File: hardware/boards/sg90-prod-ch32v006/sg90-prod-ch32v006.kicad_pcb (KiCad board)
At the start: 4 copper layers, 12.1 x 9.6 mm, 31 parts, among them J1 Servo Input, J2 Motor, J3 Debug, J4 Potentiometer, U1 TLV76733DRVR, U4 DRV8837, U5 CH32V006F8U6, U6 74LVC2G241GS,115

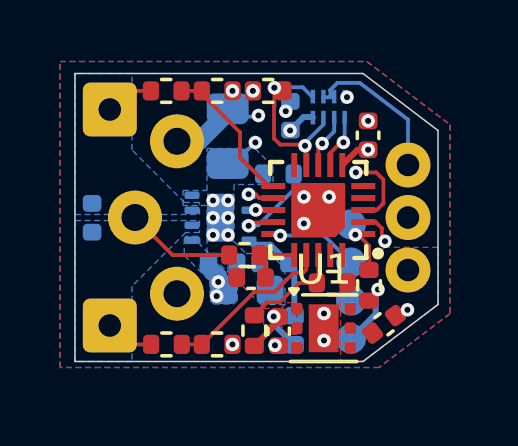
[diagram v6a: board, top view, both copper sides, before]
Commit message: fix ch32v006 footprint. it should be smd instead of th
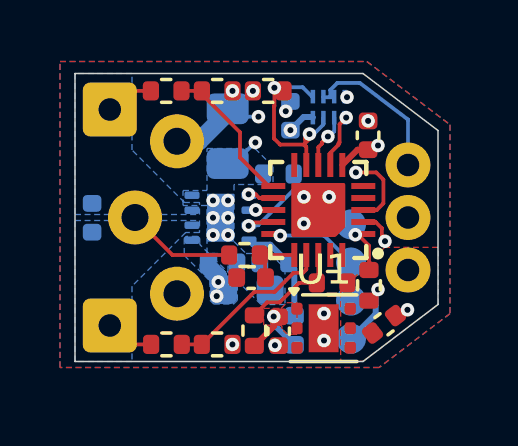
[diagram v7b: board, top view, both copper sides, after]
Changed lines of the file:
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@@
 		(sheetname "/")
 		(sheetfile "sg90-prod-ch32v006.kicad_sch")
-		(attr through_hole)
+		(attr smd)
 		(fp_line
 			(start 1.6 -1.6)
@@
 			(layer "F.Fab")
 		)
+		(fp_text user "${REFERENCE}"
+			(at 0 0 90)
+			(layer "F.Fab")
+			(effects
+				(font
+					(size 1 1)
+					(thickness 0.15)
+				)
+			)
+		)
 		(pad "1" smd rect
 			(at -0.8 1.5 90)
@@
 	)
 	(via
-		(at 109.770389 92.739435)
+		(at 110.1 92.6)
 		(size 0.45)
 		(drill 0.2)
@@
 	)
 	(via
-		(at 107.17 92.1)
+		(at 107.18 92.09)
 		(size 0.45)
 		(drill 0.2)
@@
 	)
 	(segment
-		(start 107.91 91.65)
-		(end 107.93 91.67)
-		(width 0.2)
-		(layer "B.Cu")
-		(net 6)
-	)
-	(segment
 		(start 110.1 97.4)
 		(end 110.025003 97.474997)
@@
 	)
 	(segment
-		(start 107.17 92.1)
-		(end 107.62 91.65)
+		(start 107.91 91.65)
+		(end 107.93 91.67)
 		(width 0.2)
 		(layer "B.Cu")
@@
 	)
 	(segment
-		(start 110.025003 98.214997)
-		(end 109.2 99.04)
+		(start 107.18 92.09)
+		(end 107.62 91.65)
 		(width 0.2)
 		(layer "B.Cu")
@@
 	)
 	(segment
+		(start 110.025003 98.214997)
+		(end 109.2 99.04)
+		(width 0.2)
+		(layer "B.Cu")
+		(net 6)
+	)
+	(segment
 		(start 106.622843 98.3)
 		(end 106.622843 98.557843)
@@
 	)
 	(segment
-		(start 108.238595 92.532886)
-		(end 108.237181 92.532886)
+		(start 108.237181 92.532886)
+		(end 108.11 92.660067)
 		(width 0.127)
 		(layer "F.Cu")
@@
 	)
 	(segment
-		(start 108.237181 92.532886)
-		(end 108.11 92.660067)
+		(start 108.430004 92.299417)
+		(end 108.237181 92.49224)
 		(width 0.127)
 		(layer "F.Cu")
@@
 		(net 7)
 	)
+	(segment
+		(start 108.237181 92.49224)
+		(end 108.237181 92.532886)
+		(width 0.127)
+		(layer "F.Cu")
+		(net 7)
+	)
 	(via
-		(at 108.238595 92.532886)
+		(at 108.430004 92.299417)
 		(size 0.45)
 		(drill 0.2)
@@
 	)
 	(segment
-		(start 108.238595 92.532886)
+		(start 108.472064 92.299417)
 		(end 108.64 92.131481)
 		(width 0.127)
@@
 	)
 	(segment
-		(start 108.782793 92.576294)
-		(end 108.51 92.849087)
+		(start 108.430004 92.299417)
+		(end 108.472064 92.299417)
+		(width 0.127)
+		(layer "B.Cu")
+		(net 7)
+	)
+	(segment
+		(start 108.818504 92.497998)
+		(end 108.782793 92.533709)
+		(width 0.127)
+		(layer "F.Cu")
+		(net 8)
+	)
+	(segment
+		(start 108.51 92.849087)
+		(end 108.51 93.25)
 		(width 0.127)
 		(layer "F.Cu")
@@
 	)
 	(segment
-		(start 108.51 92.849087)
-		(end 108.51 93.25)
+		(start 109.040002 91.67)
+		(end 108.818504 91.891498)
 		(width 0.127)
 		(layer "F.Cu")
@@
 	)
 	(segment
-		(start 108.946502 92.497998)
+		(start 108.818504 91.891498)
 		(end 108.818504 92.497998)
 		(width 0.127)
@@
 	)
 	(segment
-		(start 108.818504 92.497998)
-		(end 108.782793 92.533709)
+		(start 108.782793 92.576294)
+		(end 108.51 92.849087)
 		(width 0.127)
 		(layer "F.Cu")
@@
 	)
 	(via
-		(at 108.946502 92.497998)
+		(at 109.040002 91.67)
 		(size 0.45)
 		(drill 0.2)
@@
 	)
 	(segment
-		(start 108.99 92.4545)
-		(end 108.99 91.7)
+		(start 109.040002 91.67)
+		(end 109.02 91.67)
 		(width 0.127)
 		(layer "B.Cu")
@@
 	)
 	(segment
-		(start 108.946502 92.497998)
-		(end 108.99 92.4545)
+		(start 109.02 91.67)
+		(end 108.99 91.7)
 		(width 0.127)
 		(layer "B.Cu")
@@
 	)
 	(via
-		(at 106.115 91.6)
+		(at 106.115 91.64)
 		(size 0.45)
 		(drill 0.2)
@@
 	)
 	(segment
-		(start 106.115 91.645)
-		(end 107.551498 93.081498)
+		(start 106.115 91.64)
+		(end 106.115 92.015)
 		(width 0.127)
 		(layer "In2.Cu")
@@
 	)
 	(segment
-		(start 110.332581 95.52588)
-		(end 110.332581 95.790872)
-		(width 0.127)
-		(layer "In2.Cu")
-		(net 19)
-	)
-	(segment
-		(start 110.1855 93.732476)
-		(end 110.1855 95.378799)
+		(start 106.115 92.015)
+		(end 107.181498 93.081498)
 		(width 0.127)
 		(layer "In2.Cu")
@@
 	)
 	(segment
-		(start 107.551498 93.081498)
+		(start 107.181498 93.081498)
 		(end 109.534522 93.081498)
 		(width 0.127)
@@
 	)
 	(segment
-		(start 106.115 91.6)
-		(end 106.115 91.645)
+		(start 110.332581 95.52588)
+		(end 110.332581 95.790872)
 		(width 0.127)
 		(layer "In2.Cu")
@@
 	)
 	(segment
-		(start 107.627679 92.570124)
-		(end 107.666649 92.609094)
+		(start 110.1855 93.732476)
+		(end 110.1855 95.378799)
+		(width 0.127)
+		(layer "In2.Cu")
+		(net 19)
+	)
+	(segment
+		(start 107.71 92.64793)
+		(end 107.71 93.25)
 		(width 0.127)
 		(layer "F.Cu")
@@
 	)
 	(segment
-		(start 106.646135 90.675)
+		(start 107.815 92.21753)
+		(end 107.815 92.382803)
+		(width 0.127)
+		(layer "F.Cu")
+		(net 20)
+	)
+	(segment
+		(start 106.635025 91.296663)
 		(end 106.646135 91.285553)
 		(width 0.127)
@@
 	(segment
 		(start 106.646135 91.285553)
-		(end 106.635025 91.296663)
+		(end 106.646135 90.675)
+		(width 0.127)
+		(layer "F.Cu")
+		(net 20)
+	)
+	(segment
+		(start 106.839144 92.570124)
+		(end 106.635025 92.366005)
 		(width 0.127)
 		(layer "F.Cu")
@@
 	(segment
 		(start 106.635025 92.366005)
-		(end 106.839144 92.570124)
+		(end 106.635025 91.296663)
 		(width 0.127)
 		(layer "F.Cu")
@@
 	)
 	(segment
-		(start 106.839144 92.570124)
-		(end 107.627679 92.570124)
+		(start 107.815 92.21753)
+		(end 107.671164 92.361366)
 		(width 0.127)
 		(layer "F.Cu")
@@
 	)
 	(segment
-		(start 107.666649 92.609094)
+		(start 107.671164 92.361366)
 		(end 107.671164 92.609094)
 		(width 0.127)
@@
 	)
 	(segment
-		(start 106.635025 91.296663)
-		(end 106.635025 92.366005)
+		(start 107.815 92.382803)
+		(end 107.627679 92.570124)
 		(width 0.127)
 		(layer "F.Cu")
@@
 	)
 	(segment
-		(start 107.71 92.64793)
-		(end 107.71 93.25)
+		(start 107.627679 92.570124)
+		(end 106.839144 92.570124)
 		(width 0.127)
 		(layer "F.Cu")
@@
 	)
 	(via
-		(at 107.666649 92.609094)
+		(at 107.815 92.21753)
 		(size 0.45)
 		(drill 0.2)
@@
 	)
 	(segment
-		(start 108.28 91.9)
-		(end 108.28 91.67)
+		(start 106.646135 90.675)
+		(end 106.662635 90.6585)
 		(width 0.127)
 		(layer "B.Cu")
@@
 	)
 	(segment
-		(start 106.646135 90.675)
-		(end 106.662635 90.6585)
+		(start 107.96247 92.21753)
+		(end 108.28 91.9)
 		(width 0.127)
 		(layer "B.Cu")
@@
 	)
 	(segment
-		(start 107.666649 92.513351)
-		(end 108.28 91.9)
+		(start 107.5885 90.6585)
+		(end 107.9 90.97)
 		(width 0.127)
 		(layer "B.Cu")
@@
 	)
 	(segment
-		(start 107.666649 92.609094)
-		(end 107.666649 92.513351)
+		(start 108.28 91.9)
+		(end 108.28 91.67)
 		(width 0.127)
 		(layer "B.Cu")
@@
 	)
 	(segment
-		(start 107.5885 90.6585)
-		(end 107.9 90.97)
+		(start 107.815 92.21753)
+		(end 107.96247 92.21753)
 		(width 0.127)
 		(layer "B.Cu")
@@
 			)
 		)
+	)
+	(zone
+		(net 0)
+		(net_name "")
+		(layer "In2.Cu")
+		(hatch edge 0.5)
+		(connect_pads
+			(clearance 0)
+		)
+		(min_thickness 0.25)
+		(filled_areas_thickness no)
+		(keepout
+			(tracks allowed)
+			(vias allowed)
+			(pads allowed)
+			(copperpour not_allowed)
+			(footprints allowed)
+		)
+		(placement
+			(enabled no)
+			(sheetname "/")
+		)
+		(fill
+			(thermal_gap 0.5)
+			(thermal_bridge_width 0.5)
+		)
+		(polygon
+			(pts
+				(xy 105.6 91.8) (xy 105.6 92.8) (xy 106.73 93.93) (xy 109.5 93.93) (xy 109.8 94.23) (xy 109.8 95.9)
+				(xy 110 96.1) (xy 110.604445 96.1) (xy 110.7 96.004445) (xy 110.7 95.4) (xy 110.6 95.3) (xy 110.6 93.5)
+				(xy 109.8 92.7) (xy 107.4 92.7) (xy 106.2 91.5) (xy 105.9 91.5)
+			)
+		)

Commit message: better debugger pogo pins placement and silk screen placement
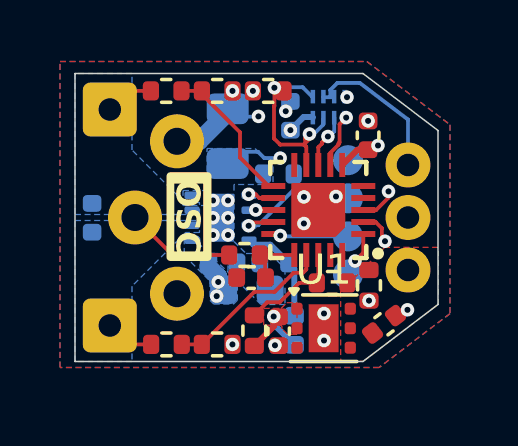
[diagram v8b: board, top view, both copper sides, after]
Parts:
- moved J3 2.14 mm to (109.1, 95.0), turned to -90 degrees
- moved NT1 0.16 mm to (105.9, 92.8), turned to 180 degrees
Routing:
- net +3V3: track 6.52 -> 5.71 mm
- net GND: track 2.21 -> 2.73 mm
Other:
- board text added: "A"
- board text added: "B"
- board text added: "OSC"
- board text added: "R S G V"
- board text added: "W"
